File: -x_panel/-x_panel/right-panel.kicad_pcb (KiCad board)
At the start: 2 copper layers, 85 x 270 mm, 12 parts

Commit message: Changes solar panels
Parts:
- added G***: LOGO, footprints:SkCubeSat-logo, F.Cu at (979.2, 60.0)
- SC2: footprint Solar_cell:Solar_Cell_Lightricity_S8040_CIC -> Solar_cell:Solar_Cell_Lightricity_S8040_CIC_Shorter_Tabs
- Sepic1: footprint Connection_Pads:2_Hirose_Pin -> Connection_Pads:DF13_Horizontal
- moved SC13 78.4 mm to (937.9, 177.9)
- moved SC12 37.2 mm to (937.9, 136.6)
- moved SC2 27.2 mm to (964.0, 121.6)
- moved Sepic1 22.8 mm to (967.0, 65.6)
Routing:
- net Net-(SC13--): track 274.3 -> 139.8 mm
- net Net-(SC2-+): track 133.9 -> 99.8 mm
- net Net-(SC12--): track 113.8 -> 92.9 mm
- net Net-(SC12-+): track 103.3 -> 93.5 mm

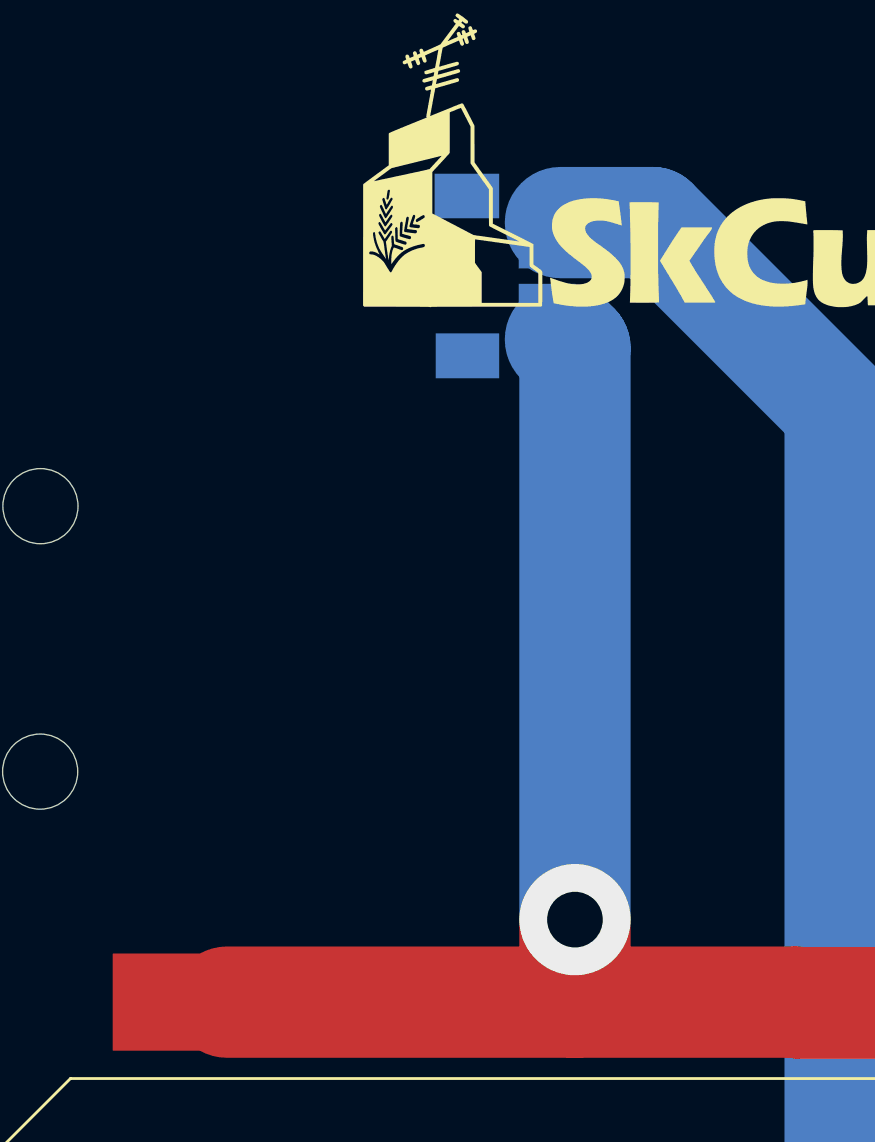
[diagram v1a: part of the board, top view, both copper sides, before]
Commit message: added schematic to +x and routed ish the schematic
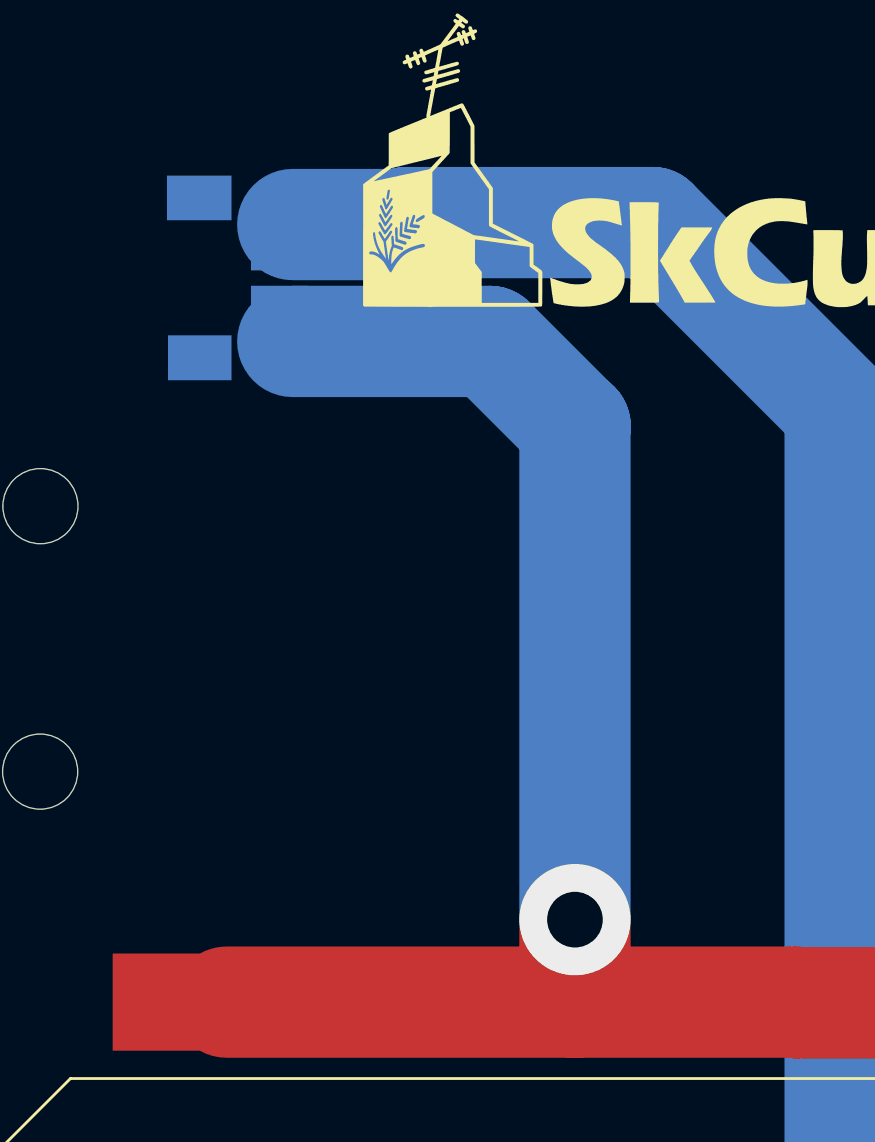
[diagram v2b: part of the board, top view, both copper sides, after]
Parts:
- moved Sepic1 9.62 mm to (957.4, 65.7)
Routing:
- net Net-(SC13--): track 139.8 -> 149.4 mm
- net Net-(SC2-+): track 99.8 -> 107.7 mm

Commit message: Updated panels based on dxf drawings from mech, need to move all holes up 5mm
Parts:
- moved Sepic1 4.59 mm to (952.8, 65.6)
- moved SC2 1.07 mm to (964.0, 122.6)
- moved SC12 0.29 mm to (937.9, 136.9)
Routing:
- net Net-(SC2-+): track 107.7 -> 57.2 mm
- net Net-(SC13--): track 149.4 -> 154.0 mm, vias 1 -> 0
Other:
- outline, holes or cut-outs redrawn
- board text added: "For Instructional Use Only."
- board text added: "SOLIDWORKS Educational Product."

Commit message: moved holes up 5mm, did what Jack said to do
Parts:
- SC2: footprint Solar_cell:Solar_Cell_Lightricity_S8040_CIC_Shorter_Tabs -> Solar_cell:Solar_Cell_Lightricity_S8040_CIC
- moved SC2 37.2 mm to (937.8, 96.3)
- moved SC13 0.92 mm to (937.8, 178.8)
- moved SC12 0.71 mm to (937.9, 137.6)
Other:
- outline, holes or cut-outs redrawn
- board text removed: "For Instructional Use Only."
- board text removed: "SOLIDWORKS Educational Product."

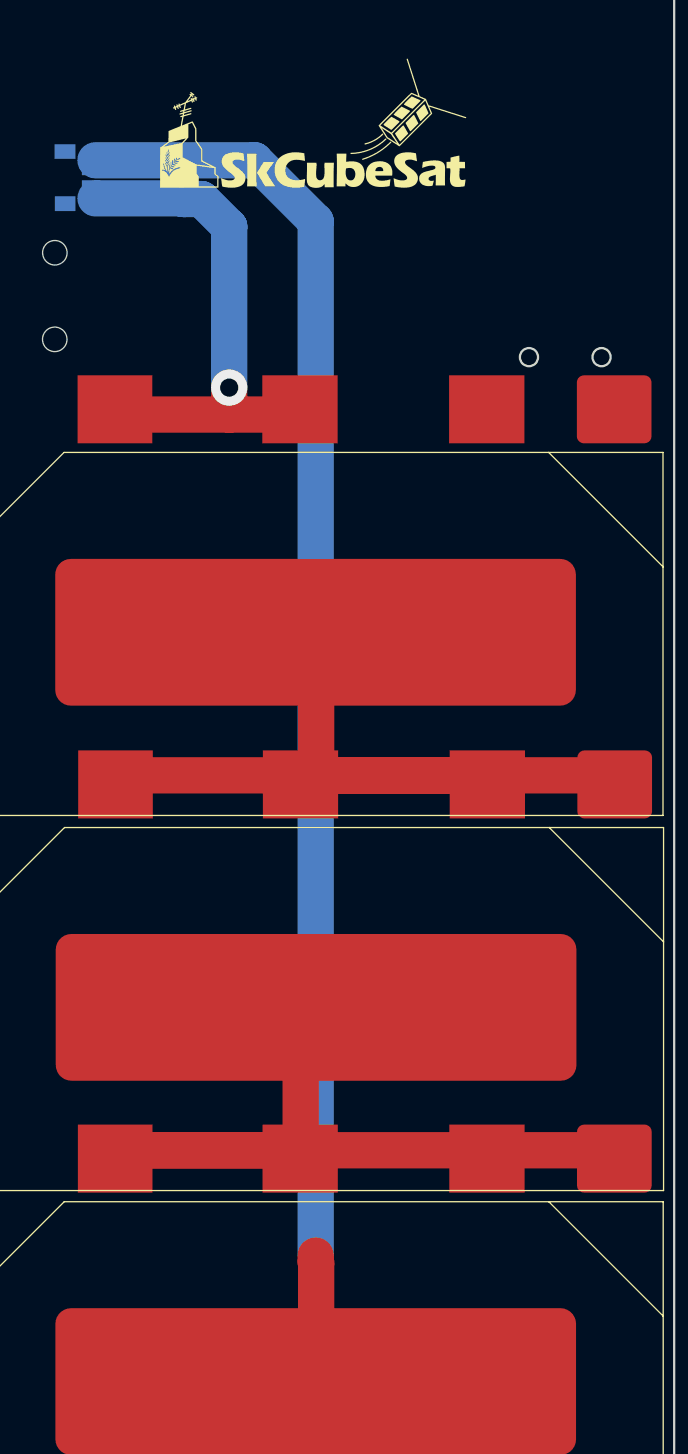
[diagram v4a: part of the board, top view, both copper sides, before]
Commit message: Moved some things around, locked some components
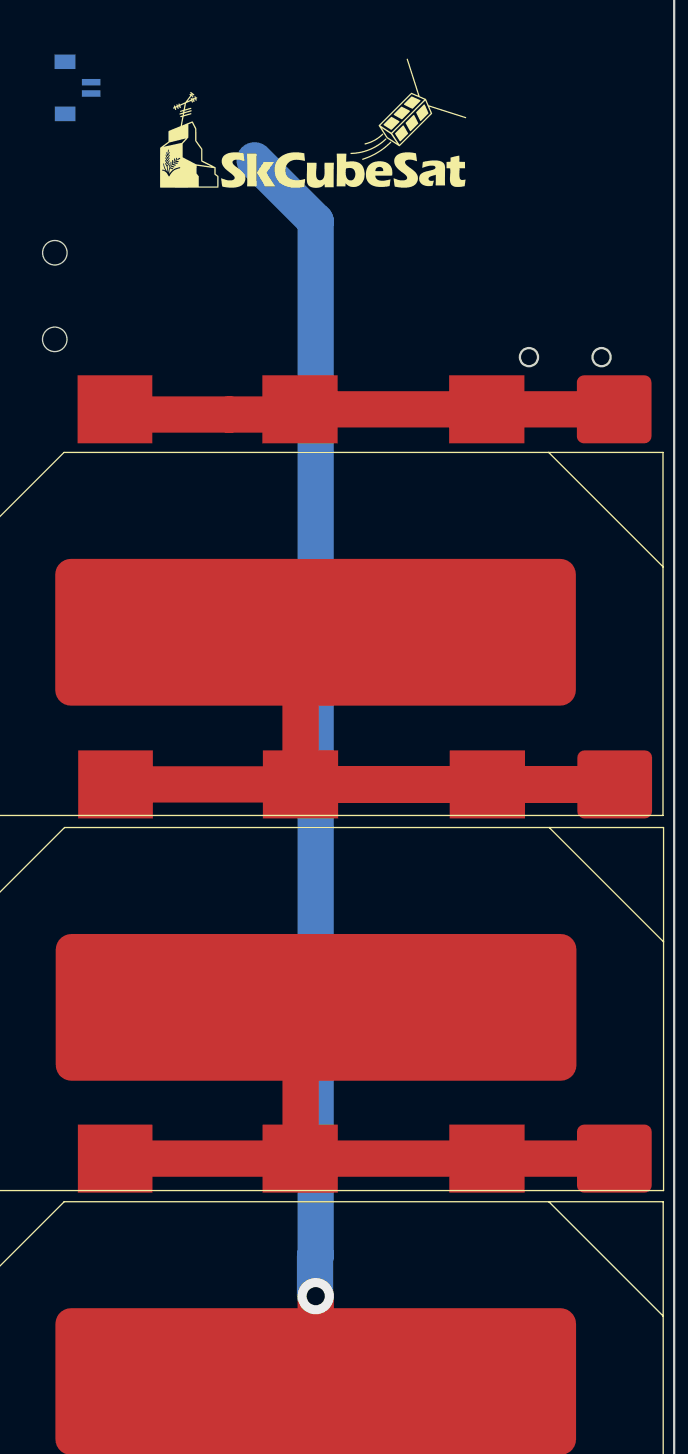
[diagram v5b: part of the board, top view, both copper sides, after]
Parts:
- moved Sepic1 9.90 mm to (952.8, 55.7)
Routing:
- net Net-(SC12-+): track 93.5 -> 123.4 mm
- net Net-(SC12--): track 92.9 -> 72.5 mm
- net Net-(SC13--): track 154.0 -> 137.4 mm, vias 0 -> 1
- net Net-(SC2-+): track 57.2 -> 55.1 mm, vias 1 -> 0
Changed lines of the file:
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@@
 	(net 4 "Net-(SC13--)")
 	(footprint "MountingHole:MountingHole_2.7mm"
+		(locked yes)
 		(layer "F.Cu")
 		(at 940.78 93.75)
@@
 	)
 	(footprint "MountingHole:MountingHole_2.7mm"
+		(locked yes)
 		(layer "F.Cu")
 		(at 940.76 222.24)
@@
 	)
 	(footprint "MountingHole:MountingHole_2.7mm"
+		(locked yes)
 		(layer "F.Cu")
 		(at 950.75 231.78)
@@
 	)
 	(footprint "Solar_cell:Solar_Cell_Lightricity_S8040_CIC"
+		(locked yes)
 		(layer "F.Cu")
 		(at 937.79 96.26 -90)
@@
 	)
 	(footprint "MountingHole:MountingHole_2.7mm"
+		(locked yes)
 		(layer "F.Cu")
 		(at 940.77 241.73)
@@
 	)
 	(footprint "MountingHole:MountingHole_2.7mm"
+		(locked yes)
 		(layer "F.Cu")
 		(at 950.77 83.8)
@@
 	)
 	(footprint "Solar_cell:Solar_Cell_Lightricity_S8040_CIC"
+		(locked yes)
 		(layer "F.Cu")
 		(at 937.85 137.59 -90)
@@
 	)
 	(footprint "Solar_cell:Solar_Cell_Lightricity_S8040_CIC"
+		(locked yes)
 		(layer "F.Cu")
 		(at 937.81 178.82 -90)
@@
 	)
 	(footprint "MountingHole:MountingHole_2.7mm"
+		(locked yes)
 		(layer "F.Cu")
 		(at 940.78 74.26)
@@
 	)
 	(footprint "MountingHole:MountingHole_2.7mm"
+		(locked yes)
 		(layer "F.Cu")
 		(at 950.78 74.26)
@@
 	)
 	(footprint "MountingHole:MountingHole_2.7mm"
+		(locked yes)
 		(layer "F.Cu")
 		(at 950.75 222.23)
@@
 	(footprint "Connection_Pads:DF13_Horizontal"
 		(layer "B.Cu")
-		(at 952.806726 65.63 90)
+		(at 952.806726 55.73 90)
 		(property "Reference" "Sepic1"
 			(at 0.19 3.95 270)
@@
 	)
 	(segment
-		(start 957.475 173.15)
-		(end 977.86 173.15)
+		(start 977.81 174.07)
+		(end 957.425 174.07)
 		(width 4)
 		(layer "F.Cu")
@@
 	)
 	(segment
-		(start 998.44 173.15)
-		(end 1012.4775 173.15)
+		(start 977.81 174.07)
+		(end 998.39 174.07)
 		(width 4)
 		(layer "F.Cu")
@@
 	)
 	(segment
-		(start 957.475 173.15)
-		(end 998.44 173.15)
+		(start 998.39 174.07)
+		(end 1012.4275 174.07)
 		(width 4)
 		(layer "F.Cu")
@@
 	)
 	(segment
-		(start 977.89 131.84)
-		(end 1012.5075 131.84)
+		(start 979.505 131.185)
+		(end 977.85 132.84)
 		(width 4)
 		(layer "F.Cu")
@@
 	)
 	(segment
-		(start 979.575 114.645)
-		(end 979.575 130.155)
+		(start 977.85 117.73)
+		(end 979.505 116.075)
 		(width 4)
 		(layer "F.Cu")
@@
 	)
 	(segment
-		(start 957.505 131.84)
-		(end 977.89 131.84)
+		(start 977.85 132.84)
+		(end 977.85 117.73)
 		(width 4)
 		(layer "F.Cu")
@@
 	)
 	(segment
-		(start 977.89 131.84)
-		(end 998.47 131.84)
+		(start 1012.4675 132.84)
+		(end 957.465 132.84)
 		(width 4)
 		(layer "F.Cu")
@@
 	)
 	(segment
-		(start 979.575 130.155)
-		(end 977.89 131.84)
+		(start 1012.4675 132.84)
+		(end 998.43 132.84)
 		(width 4)
 		(layer "F.Cu")
@@
 	)
 	(segment
-		(start 969.99 92.085)
-		(end 957.485 92.085)
+		(start 1012.4675 132.84)
+		(end 977.85 132.84)
 		(width 4)
 		(layer "F.Cu")
-		(net 3)
+		(net 2)
 	)
 	(segment
-		(start 969.99 92.085)
-		(end 969.99 89.12)
+		(start 977.79 91.51)
+		(end 998.37 91.51)
 		(width 4)
 		(layer "F.Cu")
@@
 	)
 	(segment
-		(start 977.945 92.105)
-		(end 977.925 92.085)
+		(start 969.99 92.085)
+		(end 957.485 92.085)
 		(width 4)
 		(layer "F.Cu")
@@
 	)
 	(segment
-		(start 977.925 92.085)
-		(end 969.99 92.085)
+		(start 977.945 92.105)
+		(end 977.925 92.085)
 		(width 4)
 		(layer "F.Cu")
 		(net 3)
 	)
-	(via
-		(at 969.99 89.12)
-		(size 4)
-		(drill 2)
-		(layers "F.Cu" "B.Cu")
-		(teardrops
-			(best_length_ratio 0.5)
-			(max_length 1)
-			(best_width_ratio 1)
-			(max_width 2)
-			(curved_edges no)
-			(filter_ratio 0.9)
-			(enabled yes)
-			(allow_two_segments yes)
-			(prefer_zone_connections yes)
-		)
-		(net 3)
-	)
-	(segment
-		(start 966.94 68.34)
-		(end 964.98 68.34)
-		(width 4)
-		(layer "B.Cu")
-		(net 3)
-	)
 	(segment
-		(start 969.99 71.39)
-		(end 966.94 68.34)
+		(start 998.37 91.51)
+		(end 1012.4075 91.51)
 		(width 4)
-		(layer "B.Cu")
-		(net 3)
-	)
-	(segment
-		(start 969.99 71.39)
-		(end 970 71.38)
-		(width 4)
-		(layer "B.Cu")
-		(net 3)
-	)
-	(segment
-		(start 964.91 68.27)
-		(end 955.257726 68.27)
-		(width 4)
-		(layer "B.Cu")
-		(net 3)
-	)
-	(segment
-		(start 964.98 68.34)
-		(end 964.91 68.27)
-		(width 4)
-		(layer "B.Cu")
+		(layer "F.Cu")
 		(net 3)
 	)
 	(segment
-		(start 969.99 89.12)
-		(end 969.99 71.39)
+		(start 977.925 92.085)
+		(end 969.99 92.085)
 		(width 4)
-		(layer "B.Cu")
+		(layer "F.Cu")
 		(net 3)
 	)
 	(segment
-		(start 979.52 185.48)
-		(end 979.575 185.535)
+		(start 979.525 189.225)
+		(end 979.525 198.635)
 		(width 4)
 		(layer "F.Cu")
 		(net 4)
 	)
+	(via
+		(at 979.525 189.225)
+		(size 4)
+		(drill 2)
+		(layers "F.Cu" "B.Cu")
+		(net 4)
+	)
 	(segment
-		(start 979.52 184.75)
-		(end 979.52 185.48)
+		(start 979.45 189.15)
+		(end 979.45 184.82)
 		(width 4)
-		(layer "F.Cu")
+		(layer "B.Cu")
 		(net 4)
 	)
 	(segment
-		(start 979.575 185.535)
-		(end 979.575 197.715)
+		(start 979.525 189.225)
+		(end 979.45 189.15)
 		(width 4)
-		(layer "F.Cu")
+		(layer "B.Cu")
 		(net 4)
 	)
@@
 	)
 	(segment
-		(start 972.790111 64.069)
-		(end 955.257726 64.069)
+		(start 979.45 184.82)
+		(end 979.52 184.75)
 		(width 4)
 		(layer "B.Cu")

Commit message: changed ALOT of things, got it to a point to send mech models,solar panel harness on BS need changed
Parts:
- removed G***: LOGO, footprints:SkCubeSat-logo
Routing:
- net Net-(SC2-+): track 55.1 -> 88.4 mm, vias 0 -> 1
- net Net-(SC13--): track 137.4 -> 159.2 mm
- added copper zone on B.Cu, net Net-(SC13--)
- added copper zone on B.Cu, net Net-(SC2-+)

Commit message: Rerouted some stuff
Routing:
- net Net-(SC13--): track 159.2 -> 153.3 mm
- net Net-(SC2-+): track 88.4 -> 92.5 mm
- removed copper zone on B.Cu, net Net-(SC2-+)
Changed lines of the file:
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@@
 			(best_width_ratio 1)
 			(max_width 2)
-			(curved_edges no)
+			(curved_edges yes)
 			(filter_ratio 0.9)
 			(enabled yes)
@@
 			(prefer_zone_connections yes)
 		)
+		(net 3)
+	)
+	(segment
+		(start 954.781726 56.7175)
+		(end 957.415117 56.7175)
+		(width 0.7)
+		(layer "B.Cu")
+		(net 3)
+	)
+	(segment
+		(start 957.415117 56.7175)
+		(end 957.415117 58.15)
+		(width 0.7)
+		(layer "B.Cu")
 		(net 3)
 	)
@@
 	)
 	(segment
-		(start 979.45 189.15)
-		(end 979.45 184.82)
-		(width 4)
-		(layer "B.Cu")
-		(net 4)
-	)
-	(segment
 		(start 972.790111 64.069)
 		(end 972.629 64.069)
-		(width 4)
-		(layer "B.Cu")
-		(net 4)
-	)
-	(segment
-		(start 955.257726 53.93)
-		(end 955.257726 53.85)
 		(width 4)
 		(layer "B.Cu")
@@
 	(segment
 		(start 972.629 64.069)
-		(end 964.2 55.64)
-		(width 4)
-		(layer "B.Cu")
-		(net 4)
-	)
-	(segment
-		(start 959.94 53.95)
-		(end 955.277726 53.95)
-		(width 4)
-		(layer "B.Cu")
-		(net 4)
-	)
-	(segment
-		(start 964.2 55.64)
 		(end 962.51 53.95)
 		(width 4)
@@
 	)
 	(segment
-		(start 979.52 70.798889)
+		(start 979.45 70.728889)
 		(end 972.790111 64.069)
 		(width 4)
@@
 	)
 	(segment
-		(start 979.52 184.75)
-		(end 979.52 70.798889)
-		(width 4)
+		(start 954.781726 55.4625)
+		(end 956.2875 55.4625)
+		(width 0.7)
 		(layer "B.Cu")
 		(net 4)
 	)
 	(segment
-		(start 979.45 184.82)
-		(end 979.52 184.75)
-		(width 4)
-		(layer "B.Cu")
-		(net 4)
-	)
-	(segment
-		(start 962.51 53.95)
-		(end 959.94 53.95)
+		(start 979.45 189.15)
+		(end 979.45 70.728889)
 		(width 4)
 		(layer "B.Cu")
@@
 	)
 	(zone
-		(net 3)
-		(net_name "Net-(SC2-+)")
+		(net 4)
+		(net_name "Net-(SC13--)")
 		(layer "B.Cu")
 		(hatch edge 0.5)
-		(connect_pads
+		(priority 17540)
+		(connect_pads yes
 			(clearance 0)
 		)
-		(min_thickness 0.25)
+		(min_thickness 0.0254)
 		(filled_areas_thickness no)
 		(fill yes
@@
 		(polygon
 			(pts
-				(xy 953.52 56.32) (xy 957.87 56.51) (xy 958.81 59.53) (xy 955.97 57.46) (xy 953.46 57.45) (xy 953.46 56.32)
+				(xy 961.46497 51.95) (xy 960.361099 52.03855) (xy 959.485409 52.2789) (xy 958.780854 52.633099)
+				(xy 958.190389 53.0632) (xy 957.65697 53.53125) (xy 957.123551 53.9993) (xy 956.533086 54.4294)
+				(xy 955.828531 54.7836) (xy 954.952841 55.02395) (xy 953.848971 55.1125) (xy 953.796471 55.1125)
+				(xy 953.673971 55.4625) (xy 953.796471 55.8125) (xy 953.848971 55.8125) (xy 954.88488 55.81635)
+				(xy 955.737917 55.8268) (xy 956.453799 55.842199) (xy 957.078243 55.8609) (xy 957.65697 55.88125)
+				(xy 958.235697 55.9016) (xy 958.860141 55.9203) (xy 959.576023 55.9357) (xy 960.42906 55.94615)
+				(xy 961.46497 55.95) (xy 963.46497 55.95) (xy 963.76147 53.95) (xy 962.6 51.95)
 			)
 		)
+	)
+	(zone
+		(net 3)
+		(net_name "Net-(SC2-+)")
+		(layer "B.Cu")
+		(name "$teardrop_padvia$")
+		(hatch none 0.1)
+		(priority 30000)
+		(attr
+			(teardrop
+				(type padvia)
+			)
+		)
+		(connect_pads yes
+			(clearance 0)
+		)
+		(min_thickness 0.0254)
+		(filled_areas_thickness no)
+		(fill yes
+			(thermal_gap 0.5)
+			(thermal_bridge_width 0.5)
+			(island_removal_mode 1)
+			(island_area_min 10)
+		)
+		(polygon
+			(pts
+				(xy 955.043387 57.0675) (xy 955.114363 57.072371) (xy 955.17706 57.086464) (xy 955.230974 57.108497)
+				(xy 955.277841 57.137922) (xy 955.35457 57.219392) (xy 955.411325 57.335228) (xy 955.447262 57.493921)
+				(xy 955.458513 57.704514) (xy 955.441381 57.990648) (xy 955.432227 58.120372) (xy 957.416117 58.15)
+				(xy 956.466054 56.408297) (xy 956.356636 56.446249) (xy 956.200359 56.458372) (xy 955.948522 56.439863)
+				(xy 955.812834 56.423957) (xy 955.459944 56.38608) (xy 955.043387 56.3675)
+			)
+		)

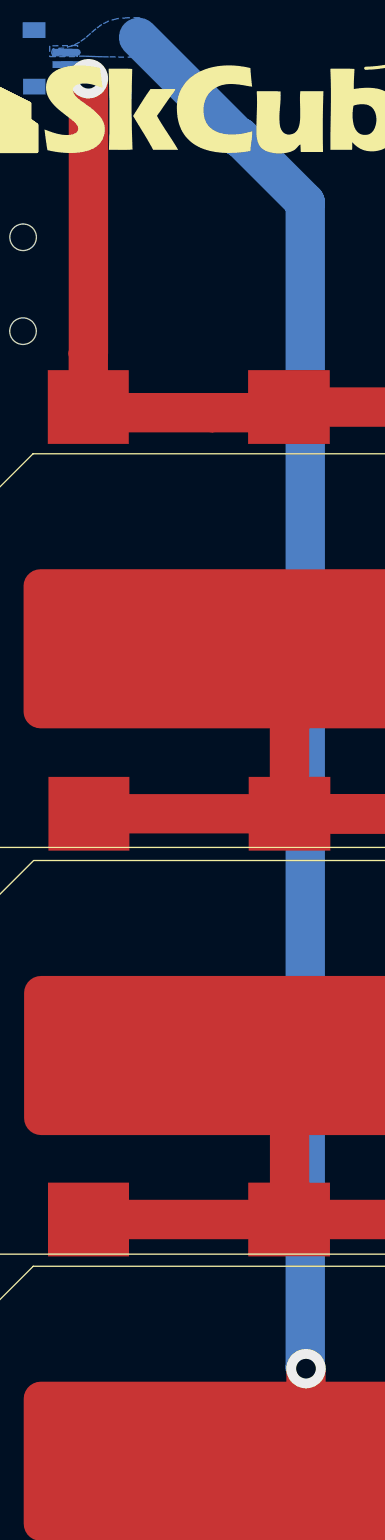
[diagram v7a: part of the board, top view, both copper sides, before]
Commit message: removed solder mask from footprint
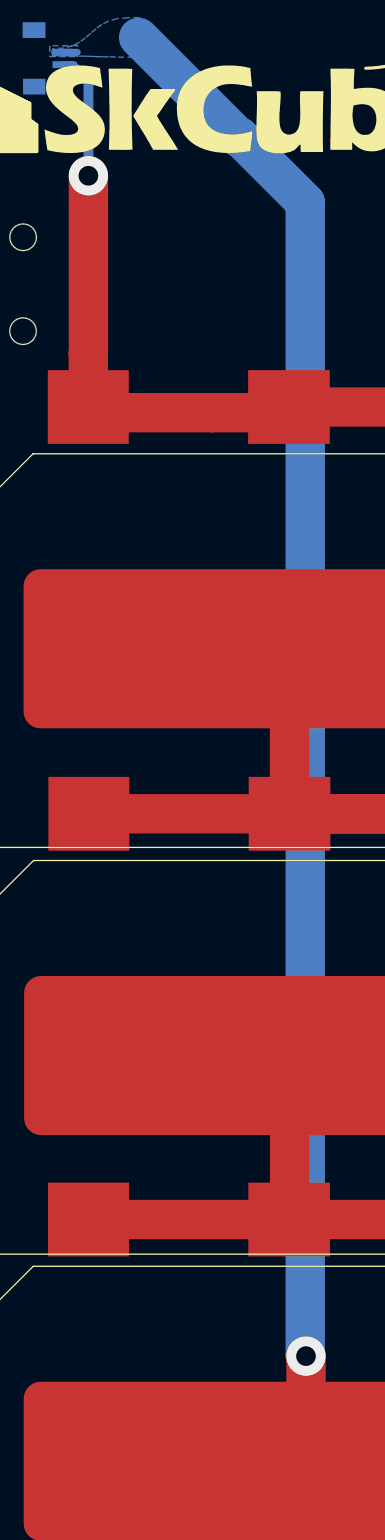
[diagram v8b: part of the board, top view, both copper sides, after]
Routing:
- net Net-(SC2-+): track 92.5 -> 91.6 mm
